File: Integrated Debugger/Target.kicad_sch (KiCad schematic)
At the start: 3 parts, among them J3 FPC socket 10P, J4 20021521-00010T1LF, SW1 RESET

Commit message: feat: add manufacturing data
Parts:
- J3: JLCPCB Part # (none) -> C2856798; LCSC Part # (none) -> C2856798; MPN (none) -> FPC-05F-10PH20
- J4: JLCPCB Part # (none) -> C2972785
- SW1: JLCPCB Part # (none) -> C843669; LCSC Part # (none) -> C843669; MPN (none) -> GT-TC029B-H025-L1N
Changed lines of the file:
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@@
+			)
+		)
+		(property "JLCPCB Part #" "C2856798"
+			(at 57.15 102.87 0)
+			(effects
+				(font
+					(size 1.27 1.27)
+				)
+				(hide yes)
+			)
+		)
+		(property "LCSC Part #" "C2856798"
+			(at 57.15 102.87 0)
+			(effects
+				(font
+					(size 1.27 1.27)
+				)
+				(hide yes)
+			)
+		)
+		(property "MPN" "FPC-05F-10PH20"
+			(at 57.15 102.87 0)
+			(effects
+				(font
+					(size 1.27 1.27)
+				)
+				(hide yes)
 			)
 		)
@@
 		(property "Description" "Single Pole Single Throw (SPST) switch"
 			(at 132.08 36.83 0)
+			(effects
+				(font
+					(size 1.27 1.27)
+				)
+				(hide yes)
+			)
+		)
+		(property "JLCPCB Part #" "C843669"
+			(at 127 36.83 90)
+			(effects
+				(font
+					(size 1.27 1.27)
+				)
+				(hide yes)
+			)
+		)
+		(property "LCSC Part #" "C843669"
+			(at 127 36.83 90)
+			(effects
+				(font
+					(size 1.27 1.27)
+				)
+				(hide yes)
+			)
+		)
+		(property "MPN" "GT-TC029B-H025-L1N"
+			(at 127 36.83 90)
 			(effects
 				(font
@@
 			(effects
 				(font
+					(size 1.27 1.27)
+				)
+				(hide yes)
+			)
+		)
+		(property "JLCPCB Part #" "C2972785"
+			(at 50.8 40.64 0)
+			(effects
+				(font

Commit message: Revise schematic, add worksheet libraries
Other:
- title: Target -> Target interface
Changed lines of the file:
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@@
 	(paper "A5")
 	(title_block
-		(title "Target")
+		(title "Target interface")
 		(date "2025-08-15")
+		(rev "1.0.0")
 	)
 	(rectangle

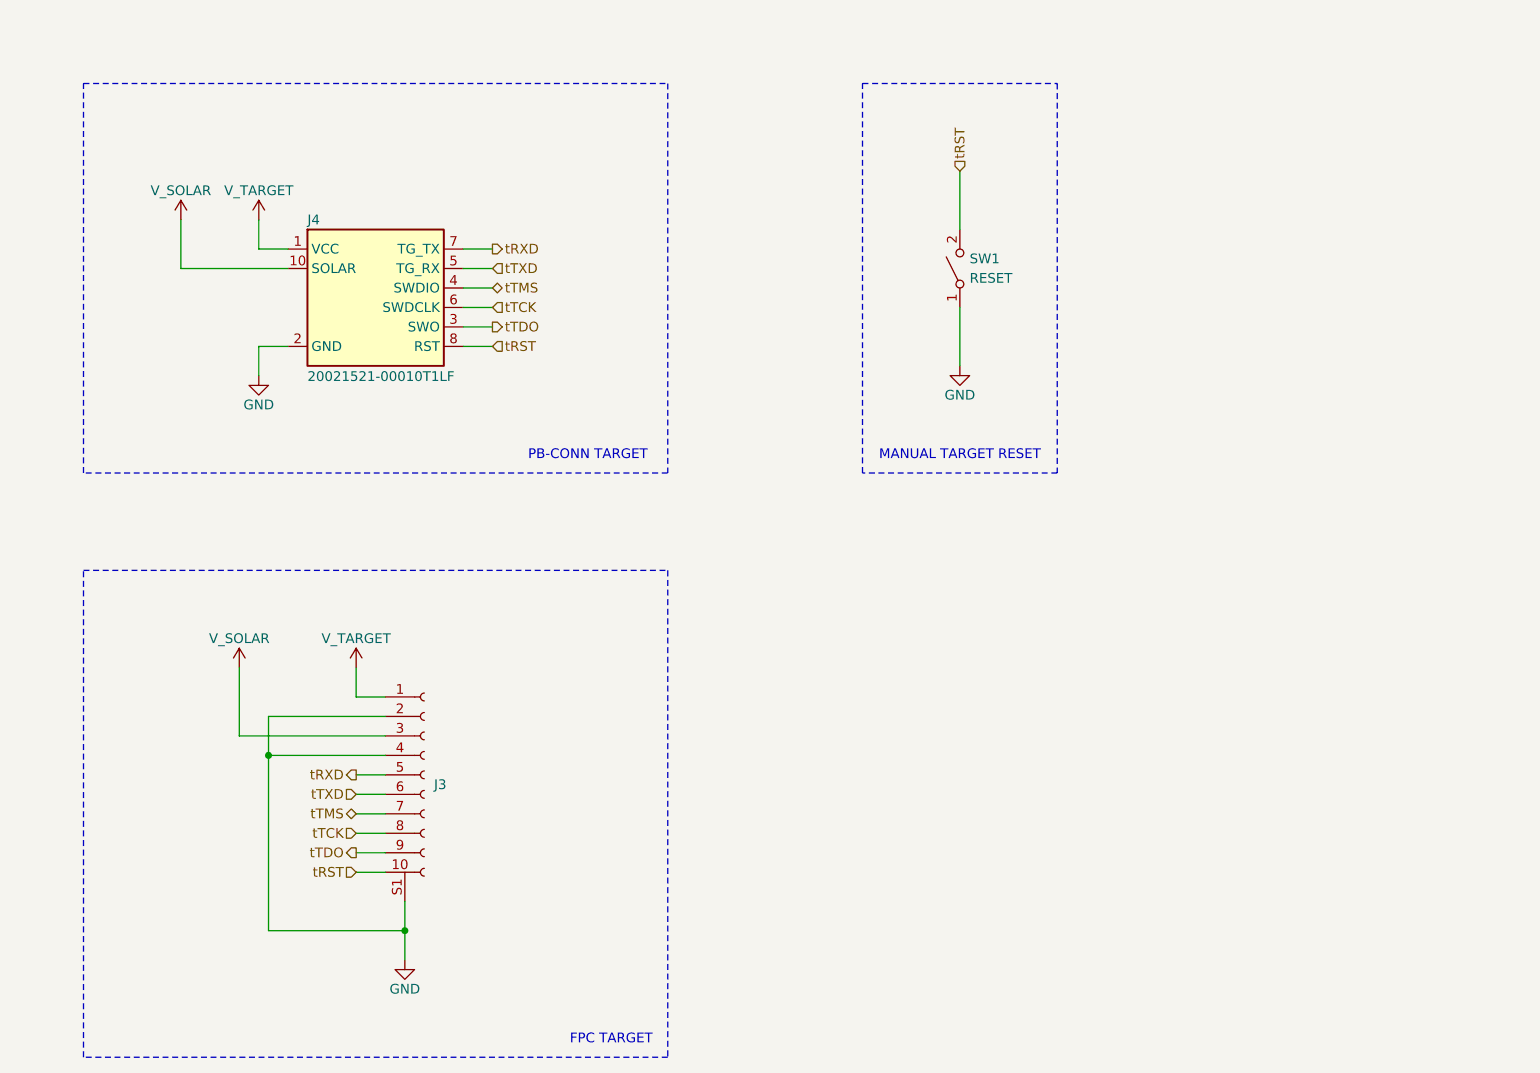
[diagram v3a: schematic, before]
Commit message: Schematic consistency improvements
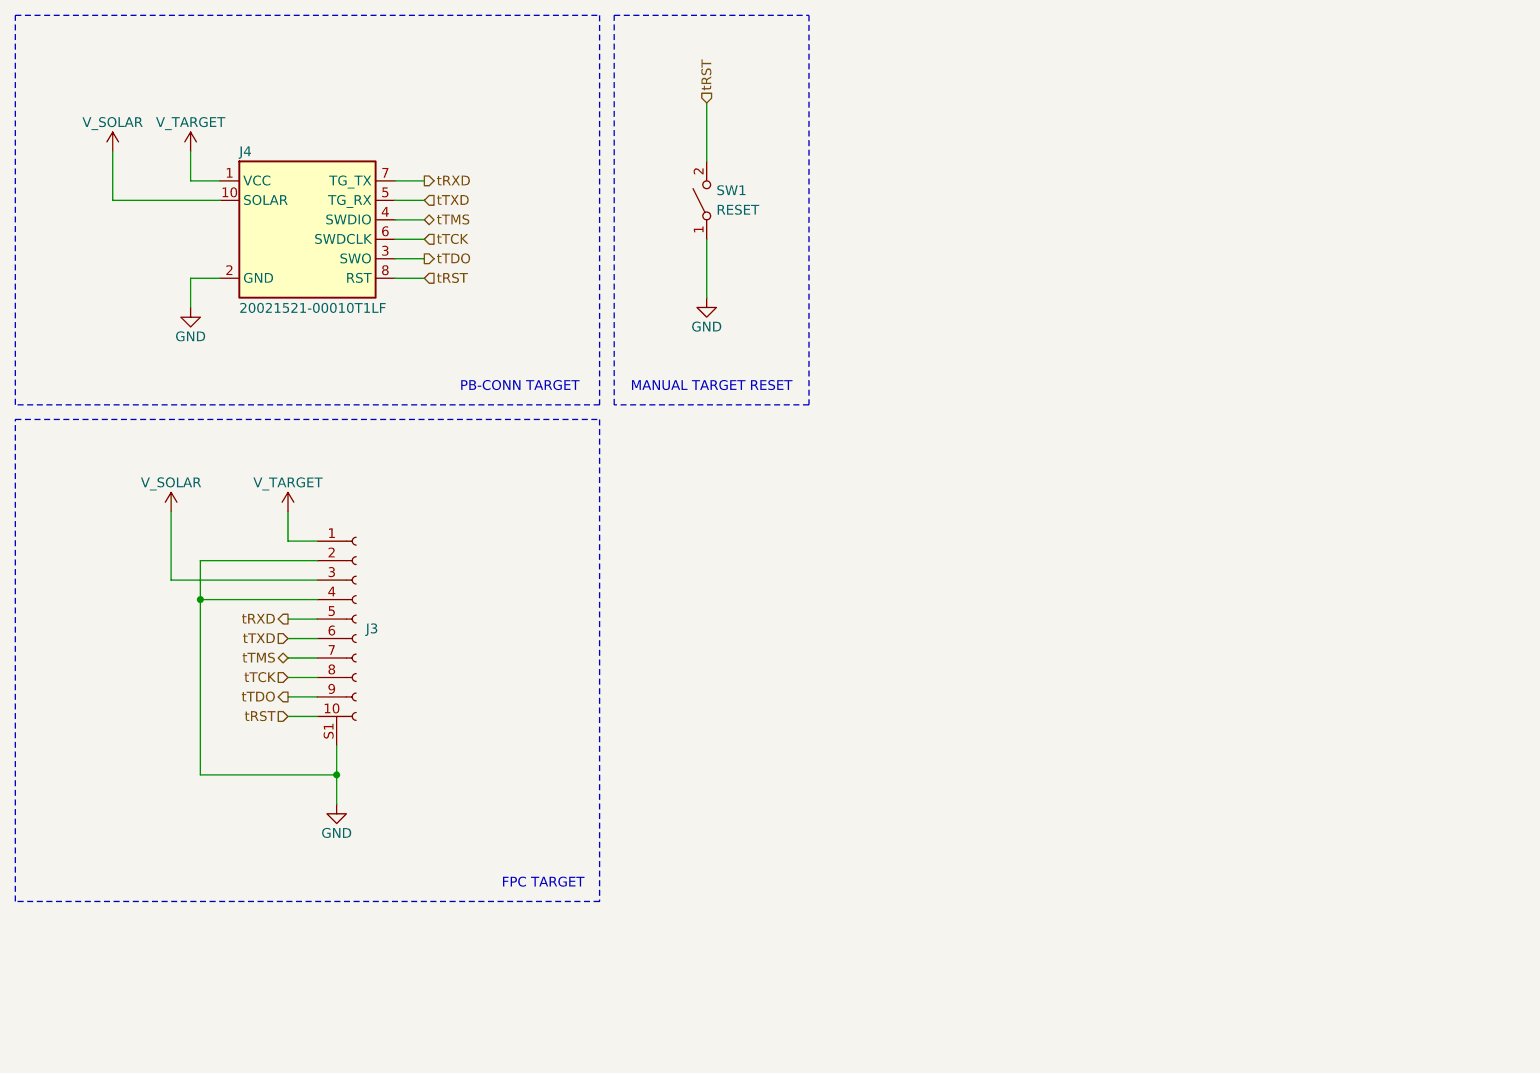
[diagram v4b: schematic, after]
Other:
- moved on the sheet: J3, J4, SW1

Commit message: PCB improvements
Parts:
- added Q1: NMOS DMN2991UDA-7B, Picoballoon ICs:X2-DFN0806-6, symbol Picoballoon ICs:NMOS DMN2991UDA-7B
- added R12: 10kΩ, Picoballoon Passives:Resistor 0201, symbol Picoballoon Passives:Resistor
- added RN1: 100Ω, Picoballoon Passives:Resistor Pack YC248-JR-07100RL, symbol Picoballoon Passives:Resistor array 8
- added U3: TXB0106RGY, Picoballoon ICs:Texas_RGY_R-PVQFN-N16_EP2.05x2.55mm, symbol Picoballoon ICs:TXB0106RGY
- renumbered SW1 to SW2
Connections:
- net GND: now also Q1.1, Q1.4, U3.17 (GND), U3.9 (GND); no longer J4.2 (GND)
- net tRST: now also RN1.1 (R1.1)
- net tRXD: now also RN1.8 (R8.1)
- net tTCK: now also RN1.4 (R4.1)
- net tTDO: now also RN1.5 (R5.1)
- net tTMS: now also RN1.3 (R3.1)
- net tTXD: now also RN1.6 (R6.1)
- new net: RN1.15 (R2.2), U3.10 (B6)
- new net: RN1.13 (R4.2), U3.12 (B4)
- new net: RN1.12 (R5.2), U3.13 (B3)
- new net: RN1.9 (R8.2), U3.16 (B1)
- new net: RN1.14 (R3.2), U3.11 (B5)
- new net: RN1.11 (R6.2), U3.14 (B2)
- new net +3.3V: U3.2 (V_{CCA}), U3.8 (OE)
- new net TARGET: R12.1
- new net i.RST: Q1.5
- new net i.RST_SEN: Q1.6
- new net i.RX: U3.1 (A1)
- new net i.TCK: U3.5 (A4)
- new net i.TDI: U3.7 (A6)
- new net i.TDO: U3.4 (A3)
- new net i.TMS: U3.6 (A5)
- new net i.TX: U3.3 (A2)
- new net tTDI: J4.2 (TDI), RN1.2 (R2.1)
- new net xRST: Q1.2, Q1.3, R12.2, RN1.16 (R1.2)
- new net xTPWR: U3.15 (V_{CCB})
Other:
- note added: "HOST <-> TARGET LEVEL SHIFTER"
- note added: "TARGET RESET LOGIC"
- title: Target interface -> Target
- moved on the sheet: J3, SW2

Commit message: Update BOM
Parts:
- renumbered R12 to R13
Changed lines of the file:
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@@
 		(dnp no)
 		(fields_autoplaced yes)
-		(property "Reference" "R12"
+		(property "Reference" "R13"
 			(at 59.69 93.0275 0)
 			(do_not_autoplace yes)
@@
 			(project "Integrated Debugger"
 				(path "/ce538ebe-fda9-4af3-9f8c-9fd5bf58f0e4/d9cee7b3-2b2b-4107-bac3-796b154ca54d"
-					(reference "R12")
+					(reference "R13")
 					(unit 1)
 				)

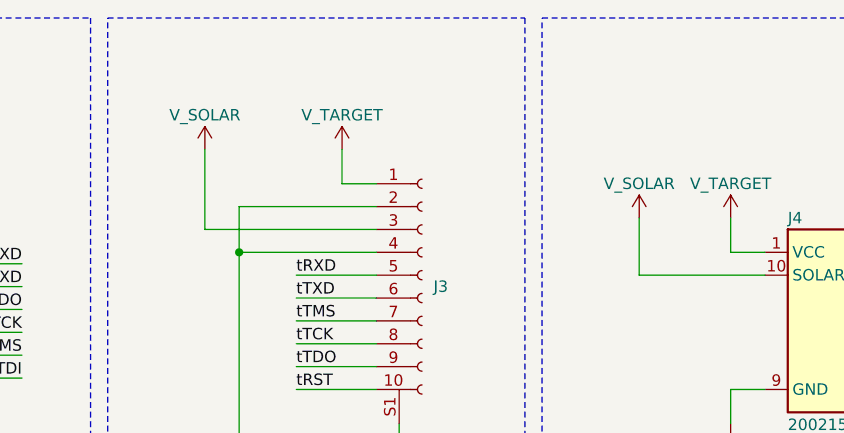
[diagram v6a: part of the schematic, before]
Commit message: feat: fix debugger bugs & impl. auxiliary power - 869b0p9f3
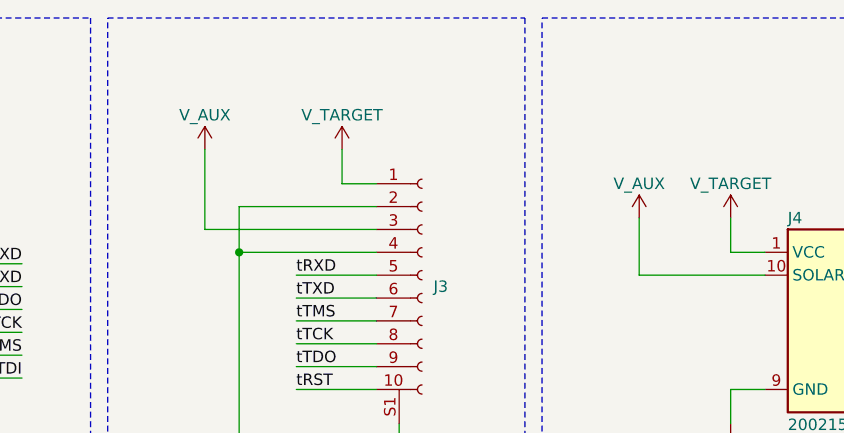
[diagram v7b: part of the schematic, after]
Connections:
- net V_SOLAR renamed V_AUX
